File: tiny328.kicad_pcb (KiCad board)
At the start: 2 copper layers, 35.3 x 22.6 mm, 25 parts, among them IC1 ATMEGA328P-A, U1 RFM12, U2 MCP1700, Y1 16MHz

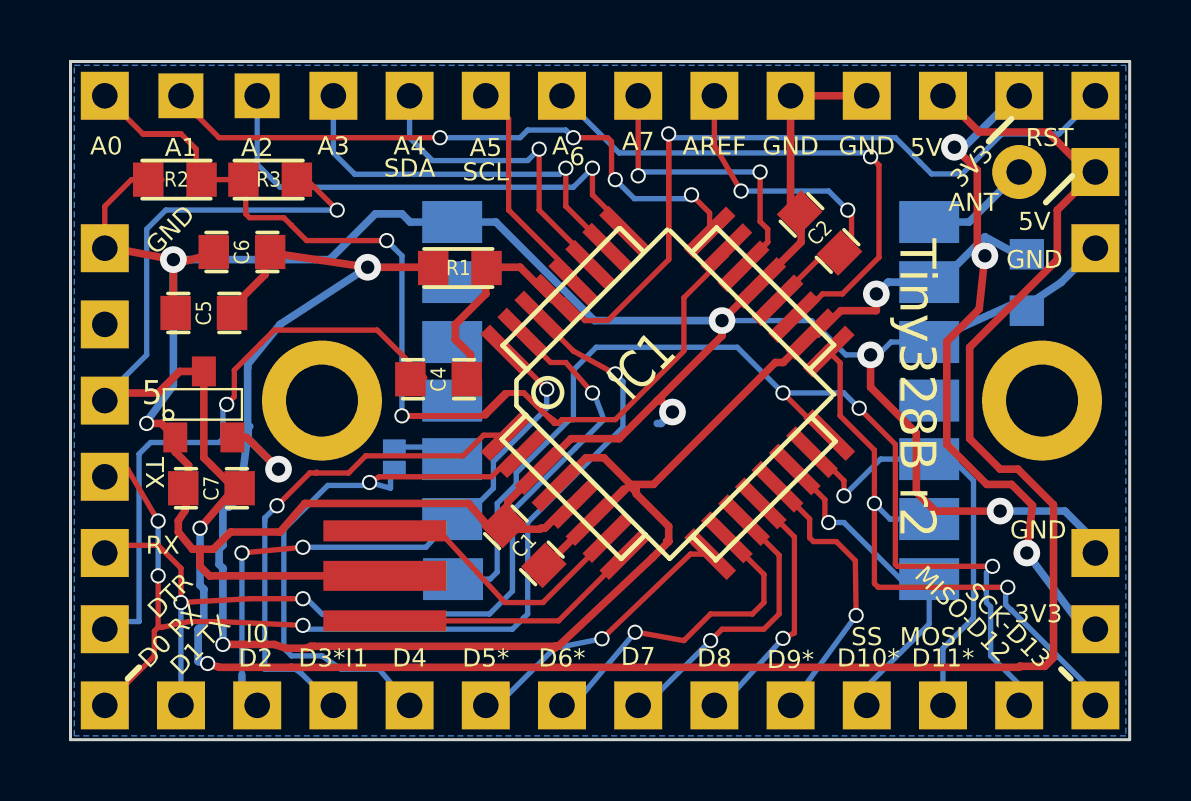
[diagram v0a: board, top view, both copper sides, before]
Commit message: change to CP2104
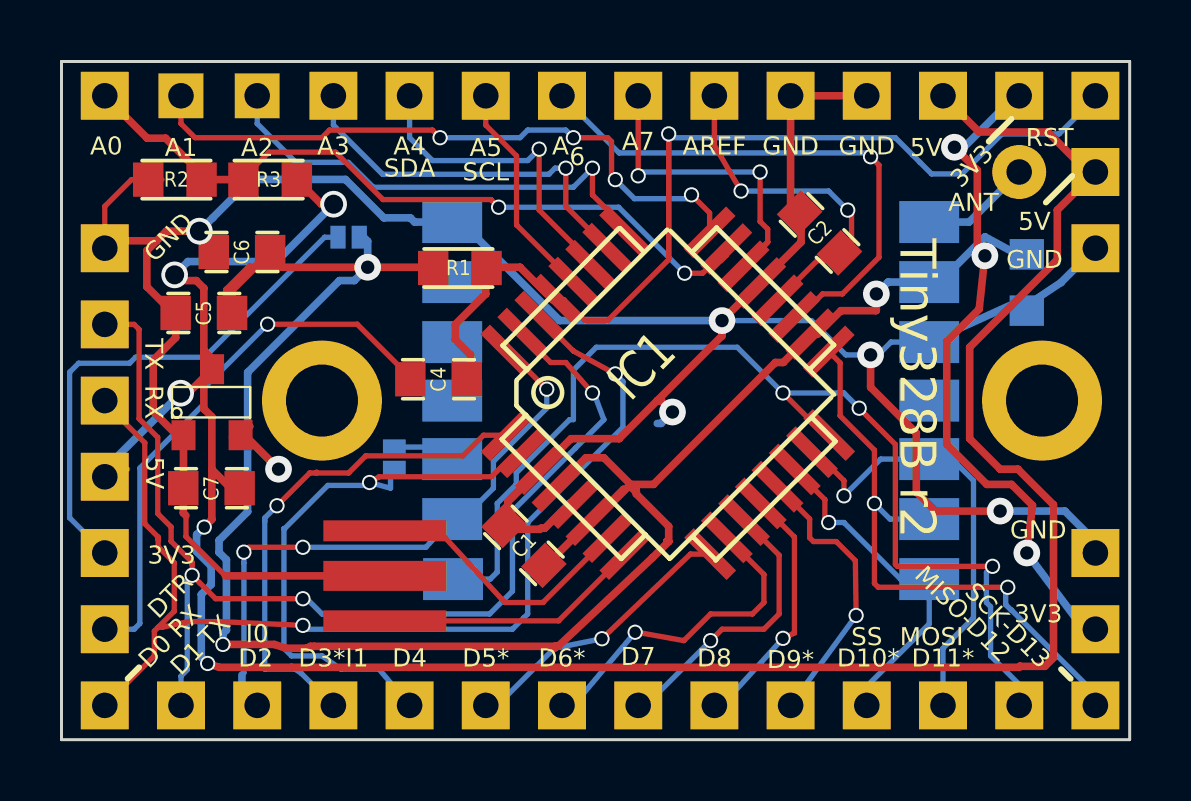
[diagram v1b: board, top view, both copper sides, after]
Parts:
- added JP10: PWR_USB, S_JUMPER_2, B.Cu at (38.1, 19.7)
- JP6: value FTDI -> CP2104
- moved U2 0.28 mm to (33.5, 25.2)
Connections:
- JP6 pad 2: /D1/TX -> Net-(JP10-Pad1)
- JP6 pad 3: /D0/RX -> +5V
- JP6 pad 4: +5V -> /D0/RX
- JP6 pad 5: (no net) -> /D1/TX
- U1 pad 11: (no net) -> Net-(U1-Pad11)
- U1 pad 4: (no net) -> Net-(U1-Pad4)
- U1 pad 5: (no net) -> Net-(U1-Pad5)
- U1 pad 6: (no net) -> Net-(U1-Pad6)
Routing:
- net /A0: track 44.5 -> 25.2 mm
- net Net-(JP10-Pad1): track 0.00 -> 17.3 mm
- net GND: track 114.9 -> 102.9 mm, vias 6 -> 5
- net /D1/TX: track 30.4 -> 37.5 mm
- net 3V3: track 95.7 -> 99.3 mm
- net /D0/RX: track 34.9 -> 37.5 mm, vias 4 -> 3
- net +5V: track 83.2 -> 84.7 mm, vias 3 -> 5
- net Net-(C4-Pad2): track 19.7 -> 18.5 mm
- net /A2: track 16.6 -> 15.8 mm
- net /A1: track 20.9 -> 21.6 mm
- net /A3: track 13.3 -> 12.8 mm
- removed copper zone on B.Cu, net GND
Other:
- board size 35.3 x 22.6 mm -> 35.6 x 22.6 mm
- board text added: "USB 3V3"
- board text removed: "5"
